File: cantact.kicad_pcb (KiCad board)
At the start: 2 copper layers, 36 x 61.1 mm, 40 parts, among them P1 USB, P2 SWD, P3 DB9, U1 STM32F042C6T6, U2 AAT3221, U3 MCP2551-I/SN, X1 16 MHz

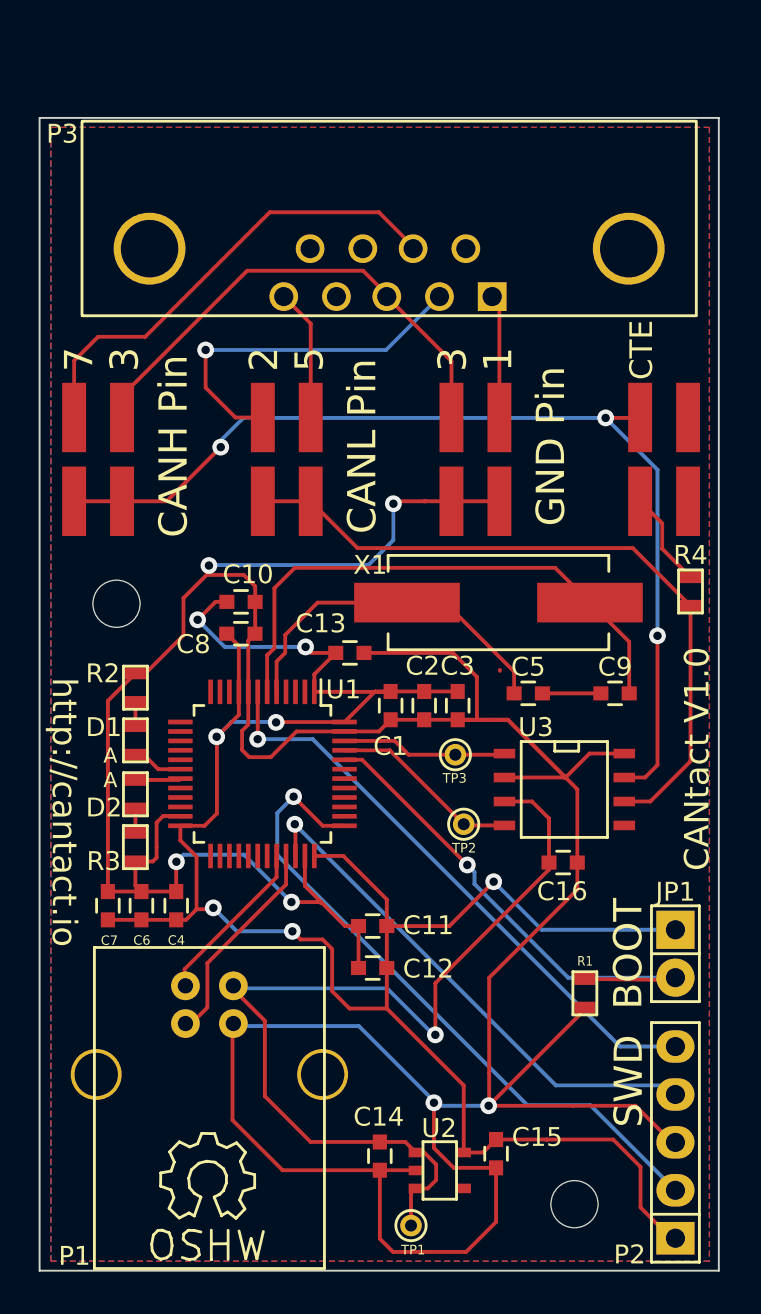
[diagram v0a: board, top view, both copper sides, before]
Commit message: feat: update project to kicad 9
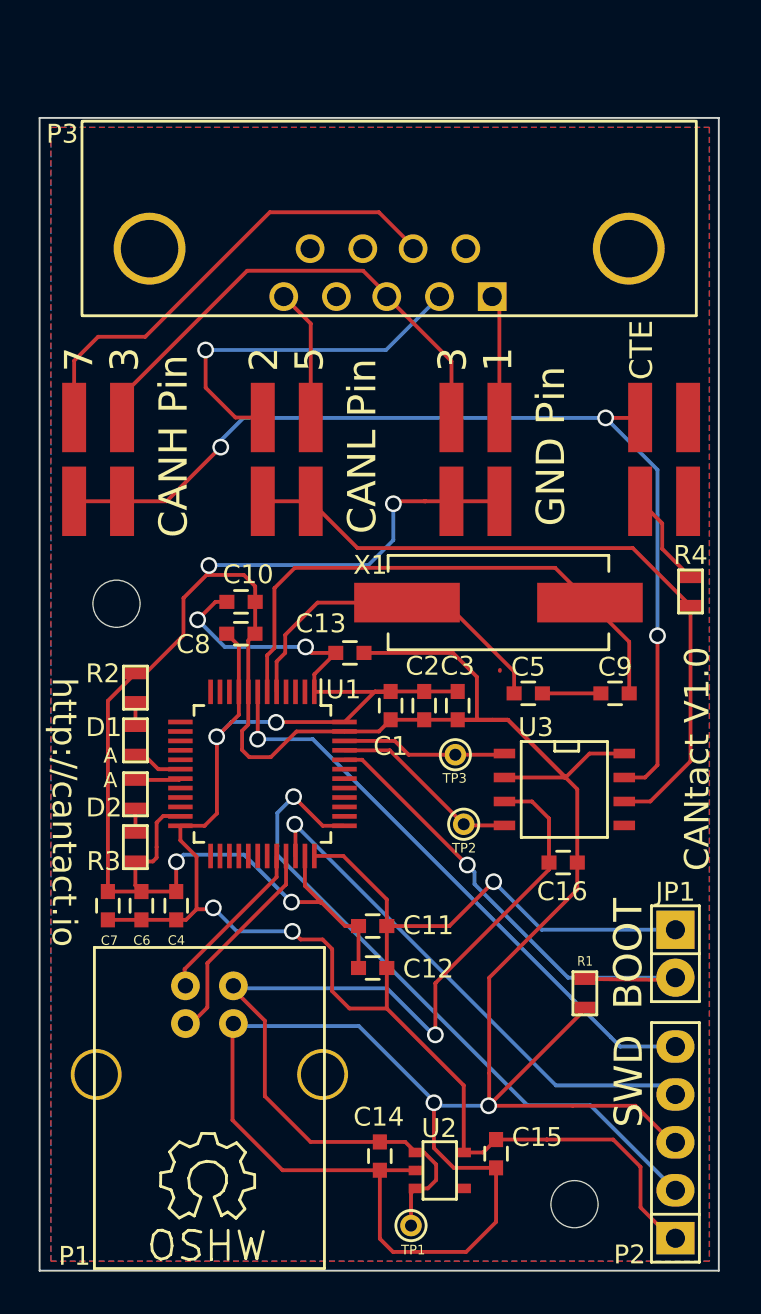
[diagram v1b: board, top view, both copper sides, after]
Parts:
- D1: value LED -> LED-GREEN
- D2: value LED -> LED-RED
- R2, R3: value R -> 120
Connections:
- net +3.3V renamed +3V3
- JP2 pad 3: Net-(JP2-Pad3) -> unconnected-(JP2-Pin_3-Pad3)
- JP2 pad 4: Net-(JP2-Pad4) -> unconnected-(JP2-Pin_4-Pad4)
- P1 pad 6: Net-(P1-Pad6) -> (no net)
- P3 pad 1: /DB9_1 -> /DB9_5
- P3 pad 2: /DB9_2 -> unconnected-(P3-Pad2)
- P3 pad 4: Net-(P3-Pad4) -> /DB9_2
- P3 pad 5: /DB9_5 -> /DB9_1
- P3 pad 6: Net-(P3-Pad6) -> unconnected-(P3-Pad6)
- P3 pad 7: /DB9_7 -> unconnected-(P3-Pad7)
- P3 pad 8: Net-(P3-Pad8) -> /DB9_7
- P3 pad 9: Net-(P3-Pad9) -> unconnected-(P3-Pad9)
- U1 pad 10: Net-(U1-Pad10) -> unconnected-(U1-PA0-Pad10)
- U1 pad 11: Net-(U1-Pad11) -> unconnected-(U1-PA1-Pad11)
- U1 pad 12: Net-(U1-Pad12) -> unconnected-(U1-PA2-Pad12)
- U1 pad 13: Net-(U1-Pad13) -> unconnected-(U1-PA3-Pad13)
- U1 pad 14: Net-(U1-Pad14) -> unconnected-(U1-PA4-Pad14)
- U1 pad 15: Net-(U1-Pad15) -> unconnected-(U1-PA5-Pad15)
- U1 pad 16: Net-(U1-Pad16) -> unconnected-(U1-PA6-Pad16)
- U1 pad 17: Net-(U1-Pad17) -> unconnected-(U1-PA7-Pad17)
- U1 pad 2: Net-(U1-Pad2) -> unconnected-(U1-PC13-Pad2)
- U1 pad 20: Net-(U1-Pad20) -> unconnected-(U1-PB2-Pad20)
- U1 pad 21: Net-(U1-Pad21) -> unconnected-(U1-PB10-Pad21)
- U1 pad 22: Net-(U1-Pad22) -> unconnected-(U1-PB11-Pad22)
- U1 pad 25: Net-(U1-Pad25) -> unconnected-(U1-PB12-Pad25)
- U1 pad 26: Net-(U1-Pad26) -> unconnected-(U1-PB13-Pad26)
- U1 pad 27: Net-(U1-Pad27) -> unconnected-(U1-PB14-Pad27)
- U1 pad 28: Net-(U1-Pad28) -> unconnected-(U1-PB15-Pad28)
- U1 pad 29: Net-(U1-Pad29) -> unconnected-(U1-PA8-Pad29)
- U1 pad 3: Net-(U1-Pad3) -> unconnected-(U1-PC14-OSC32_IN-Pad3)
- U1 pad 30: Net-(U1-Pad30) -> unconnected-(U1-PA9-Pad30)
- U1 pad 31: Net-(U1-Pad31) -> unconnected-(U1-PA10-Pad31)
- U1 pad 38: Net-(U1-Pad38) -> unconnected-(U1-PA15-Pad38)
- U1 pad 39: Net-(U1-Pad39) -> unconnected-(U1-PB3-Pad39)
- U1 pad 4: Net-(U1-Pad4) -> unconnected-(U1-PC15-OSC32_OUT-Pad4)
- U1 pad 40: Net-(U1-Pad40) -> unconnected-(U1-PB4-Pad40)
- U1 pad 41: Net-(U1-Pad41) -> unconnected-(U1-PB5-Pad41)
- U1 pad 42: Net-(U1-Pad42) -> unconnected-(U1-PB6-Pad42)
- U1 pad 43: Net-(U1-Pad43) -> unconnected-(U1-PB7-Pad43)
- U3 pad 1: /CAN_TX -> /CAN_RX
- U3 pad 4: /CAN_RX -> /CAN_TX
- U3 pad 5: Net-(U3-Pad5) -> unconnected-(U3-Vref-Pad5)
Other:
- net class Default removed
- net class Mounting Hole removed

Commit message: feat(hw):  schematic & pcb updated
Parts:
- turned D1 to -90 degrees
- turned D2 to 90 degrees
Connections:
- D1 pad 2: Net-(D1-A) -> /LED_GREEN
- D2 pad 2: Net-(D2-A) -> /LED_RED
- P3 pad 1: /DB9_5 -> /DB9_1
- P3 pad 2: unconnected-(P3-Pad2) -> /DB9_2
- P3 pad 4: /DB9_2 -> unconnected-(P3-Pad4)
- P3 pad 5: /DB9_1 -> /DB9_5
- P3 pad 7: unconnected-(P3-Pad7) -> /DB9_7
- P3 pad 8: /DB9_7 -> unconnected-(P3-Pad8)
- R2 pad 2: Net-(D1-A) -> Net-(D1-K)
- R3 pad 2: Net-(D2-A) -> Net-(D2-K)
- U1 pad 18: Net-(D1-K) -> /LED_GREEN
- U1 pad 19: Net-(D2-K) -> /LED_RED
- U3 pad 1: /CAN_RX -> /CAN_TX
- U3 pad 4: /CAN_TX -> /CAN_RX
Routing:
- net /LED_GREEN: track 0.00 -> 2.70 mm
- net /LED_RED: track 0.00 -> 2.41 mm
- net Net-(D1-K): track 2.70 -> 1.27 mm
- net Net-(D2-A): track 1.28 -> 0.00 mm
- net Net-(D1-A): track 1.27 -> 0.00 mm
- net Net-(D2-K): track 2.41 -> 1.28 mm

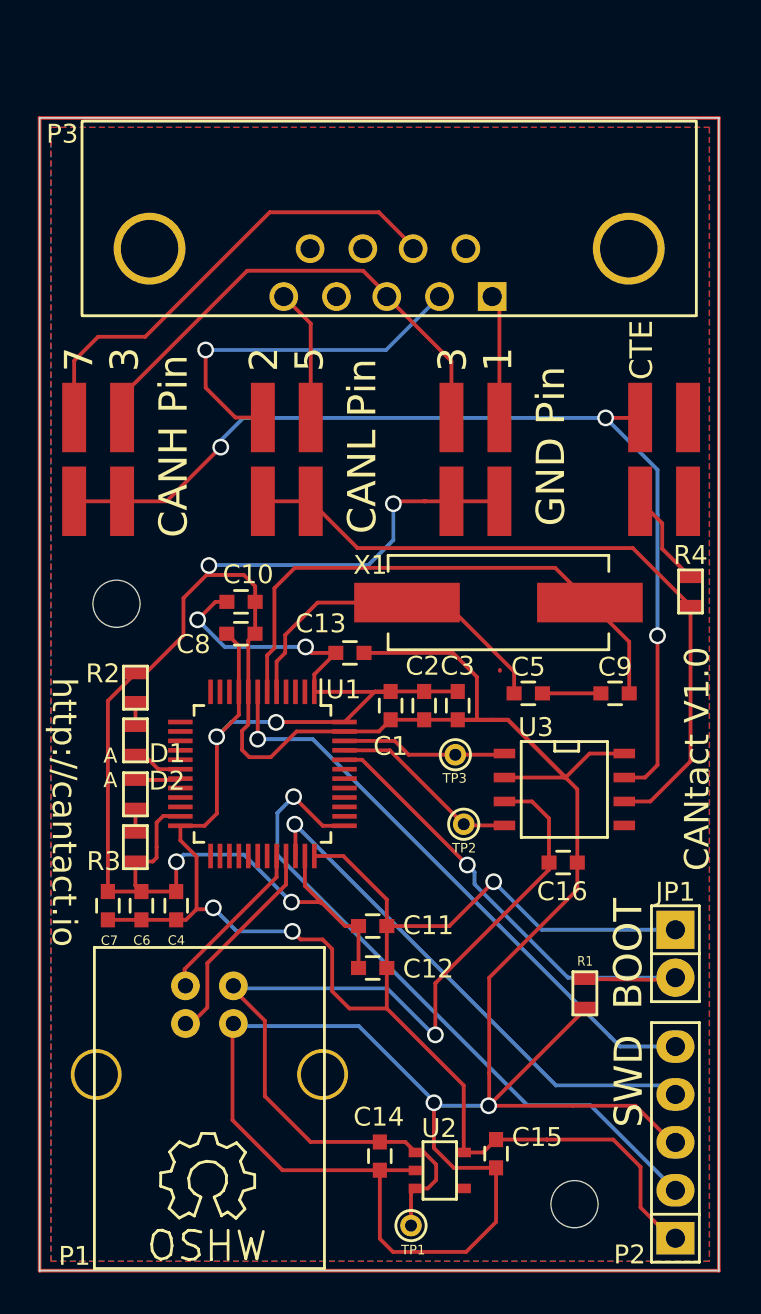
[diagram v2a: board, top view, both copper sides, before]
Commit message: feat: replace USB & RJ45 ports
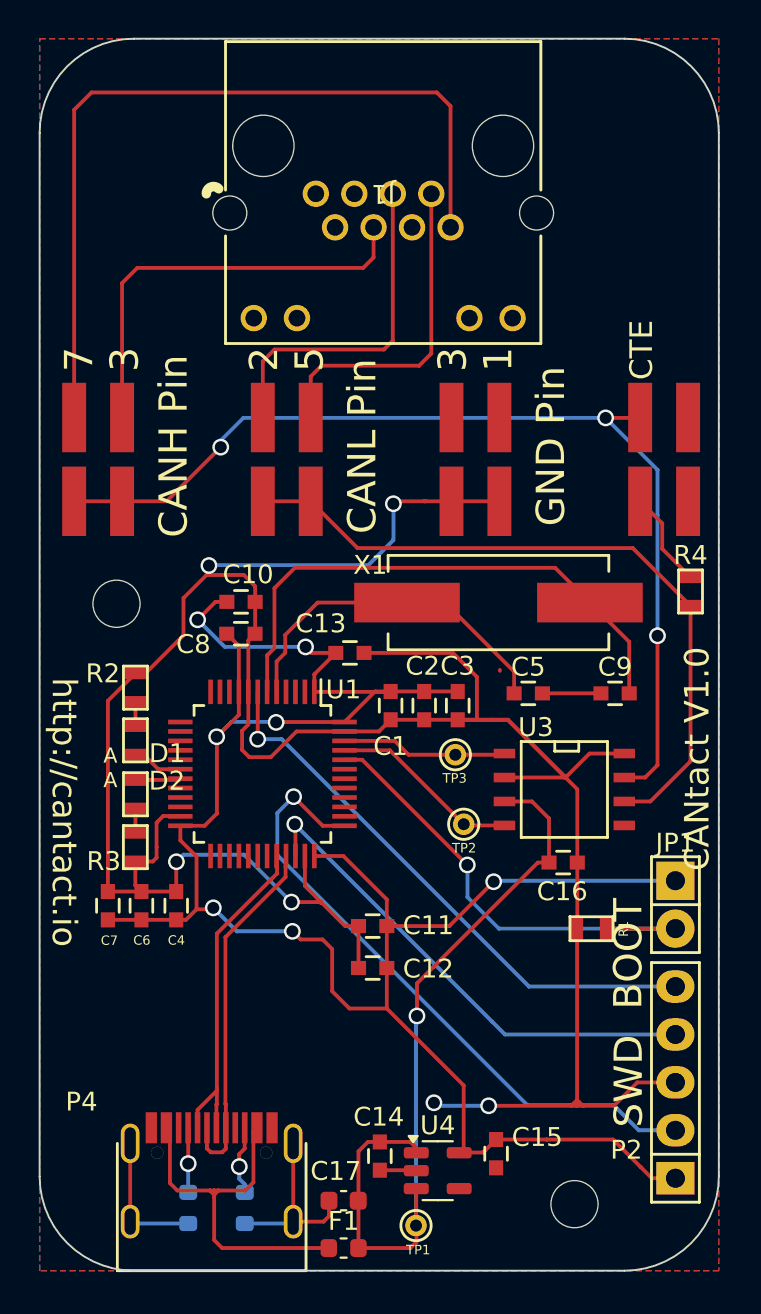
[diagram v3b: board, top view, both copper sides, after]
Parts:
- removed P1: USB, Connect:USB_B
- removed P3: DB9, Connect:DB9MC
- removed U2: AAT3221, SMD_Packages:SOT-23-5
- added C17: 10uF, Capacitor_SMD:C_0603_1608Metric, F.Cu at (140.4, 148.1)
- added F1: 750mA, Fuse:Fuse_0603_1608Metric, F.Cu at (140.4, 150.6)
- added J1: Cantact, footprints:CONN12_R-RJ45_CKM, F.Cu at (138.9, 94.7)
- added P4: USB_C_Plug_USB2.0, Footprint:C393939, F.Cu at (133.4, 145.1)
- added R10: 5k1, Resistor_SMD:R_0603_1608Metric, B.Cu at (132.2, 148.5)
- added R11: 5k1, Resistor_SMD:R_0603_1608Metric, B.Cu at (135.2, 148.5)
- added U4: XC6220B331MR-G, Package_TO_SOT_SMD:SOT-23-5, F.Cu at (145.4, 146.5)
- SYM: moved to B.Cu
- moved SYM 8.93 mm to (130.1, 138.6), turned to 180 degrees
- moved R1 3.44 mm to (153.6, 133.7), turned to 180 degrees
- moved P2 3.18 mm to (158.0, 141.8)
- moved JP1 2.60 mm to (158.0, 132.4)
- moved TP1 0.27 mm to (144.2, 149.4)
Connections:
- JP3 pad 2: /DB9_7 -> /CANH1
- JP3 pad 4: /DB9_3 -> /CANH2
- JP4 pad 2: /DB9_2 -> /CANL1
- JP4 pad 4: /DB9_5 -> /CANL2
- JP5 pad 2: /DB9_3 -> /GND1
- JP5 pad 4: /DB9_1 -> /GND2
- U1 pad 32: /USB_DM -> /D-
- U1 pad 33: /USB_DP -> /D+
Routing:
- net /CANH1: track 0.00 -> 43.4 mm
- net GND: track 212.1 -> 175.0 mm
- net /DB9_3: track 26.2 -> 0.00 mm
- net /DB9_7: track 24.9 -> 0.00 mm
- net /CANH2: track 0.00 -> 22.6 mm
- net Net-(F1-Pad1): track 0.00 -> 20.4 mm
- net /DB9_2: track 19.3 -> 0.00 mm, vias 1 -> 0
- net /D+: track 0.00 -> 19.1 mm
- net /D-: track 0.00 -> 18.3 mm
- net /CANL1: track 0.00 -> 18.1 mm
- net /CANL2: track 0.00 -> 17.5 mm
- net /USB_DP: track 11.4 -> 0.00 mm
- net /USB_DM: track 9.04 -> 0.00 mm
- net +5V: track 50.0 -> 42.4 mm
- net /DB9_1: track 7.18 -> 0.00 mm
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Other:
- board size 36 x 61.1 mm -> 36 x 65.3 mm

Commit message: refactor(hw): PCB routing
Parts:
- removed D1: LED-GREEN, SMD_Packages:SMD-0603
- removed D2: LED-RED, SMD_Packages:SMD-0603
- removed SYM: Symbol_OSHW-Logo_SilkScreen_07Jul2012, Symbols:Symbol_OSHW-Logo_SilkScreen
- removed TP1: TST, Connect:PINTST
- removed X1: 16 MHz, Crystals:Crystal_HC49-SD_SMD
- added Y1: 16 Mhz, Crystal:Crystal_SMD_2016-4Pin_2.0x1.6mm, F.Cu at (137.1, 123.4)
- C12, C3, C7: footprint Capacitors_SMD:C_0603 -> Capacitor_SMD:C_0805_2012Metric_Pad1.18x1.45mm_HandSolder
- R1, R2, R3, R4: footprint SMD_Packages:SMD-0603 -> Resistor_SMD:R_0603_1608Metric_Pad0.98x0.95mm_HandSolder
- moved R3 32.4 mm to (152.7, 106.8), turned to -90 degrees
- moved C9 20.9 mm to (134.1, 124.0)
- moved JP2 15.3 mm to (142.8, 113.4)
- moved R2 14.3 mm to (132.2, 106.9)
- moved JP4 13.2 mm to (149.8, 113.4)
- moved C5 13.2 mm to (137.0, 121.2), turned to 180 degrees
- moved R4 12.4 mm to (146.4, 115.7), turned to -90 degrees
- moved JP5 10.5 mm to (156.8, 113.4)
- moved C10 9.22 mm to (134.1, 125.5), turned to 180 degrees
- moved C8 9.11 mm to (134.1, 127.1), turned to 180 degrees
- moved JP3 9.08 mm to (135.2, 113.4)
- moved C11 8.16 mm to (139.6, 141.3), turned to 0 degrees
- moved C13 8.08 mm to (139.7, 127.1), turned to 180 degrees
- moved U1 7.73 mm to (136.1, 133.2)
- moved C3 7.44 mm to (142.4, 128.1)
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- renumbered TP2 to CanRx, TP3 to CanTx
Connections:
- J1 pad 10: unconnected-(J1-Pad10) -> Net-(J1-Pad10)
- J1 pad 11: unconnected-(J1-Pad11) -> /LED_GREEN
- J1 pad 12: unconnected-(J1-Pad12) -> Net-(J1-Pad12)
- J1 pad 4: /CANH2 -> /CANH1
- J1 pad 7: /CANL2 -> /GND1
- J1 pad 8: /CANH1 -> unconnected-(J1-Pad8)
- J1 pad 9: unconnected-(J1-Pad9) -> /LED_RED
- JP3 pad 2: /CANH1 -> /CANH2
- JP3 pad 4: /CANH2 -> /CANH1
- R2 pad 1: GND -> Net-(J1-Pad12)
- R2 pad 2: Net-(D1-K) -> GND
- R3 pad 1: GND -> Net-(J1-Pad10)
- R3 pad 2: Net-(D2-K) -> GND
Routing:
- net GND: track 175.0 -> 57.7 mm, vias 6 -> 9
- net /LED_RED: track 2.41 -> 43.0 mm, vias 0 -> 1
- net /LED_GREEN: track 2.70 -> 34.8 mm, vias 0 -> 1
- net /CANH1: track 43.4 -> 13.6 mm
- net Net-(JP4-Pin_1): track 37.6 -> 10.6 mm
- net Net-(JP2-Pin_2): track 53.7 -> 28.2 mm, vias 3 -> 0
- net Net-(U1-PF1-OSC_OUT): track 29.4 -> 6.47 mm
- net /CANH2: track 22.6 -> 0.00 mm
- net /GND1: track 0.00 -> 21.2 mm
- net /CANL2: track 17.5 -> 0.00 mm
- net Net-(U1-PF0-OSC_IN): track 20.3 -> 8.27 mm
- net /SWCLK: track 34.1 -> 24.8 mm
- net /D-: track 18.3 -> 11.7 mm
- net /D+: track 19.1 -> 12.7 mm
- net +3V3: track 115.4 -> 109.1 mm, vias 7 -> 4
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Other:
- board size 36 x 65.3 mm -> 36.1 x 59.9 mm
- board text added: "CANH"
- board text added: "CANL"
- board text added: "GND"
- board text removed: "2 5"
- board text removed: "3 1"
- board text removed: "7 3"
- board text removed: "A"
- board text removed: "CANH Pin"
- board text removed: "CANL Pin"
- board text removed: "CTE"
- board text removed: "GND Pin"
- board text removed: "http://cantact.io"
